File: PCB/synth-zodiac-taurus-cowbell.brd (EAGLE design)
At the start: 49 x 22 mm, 53 parts, among them Q1 NPN, Q2 NPN, SW1 Push Switch, SW2 Push Switch, U1 TL071, U2 ATTiny2313, X1 16MHz, X2 16MHz

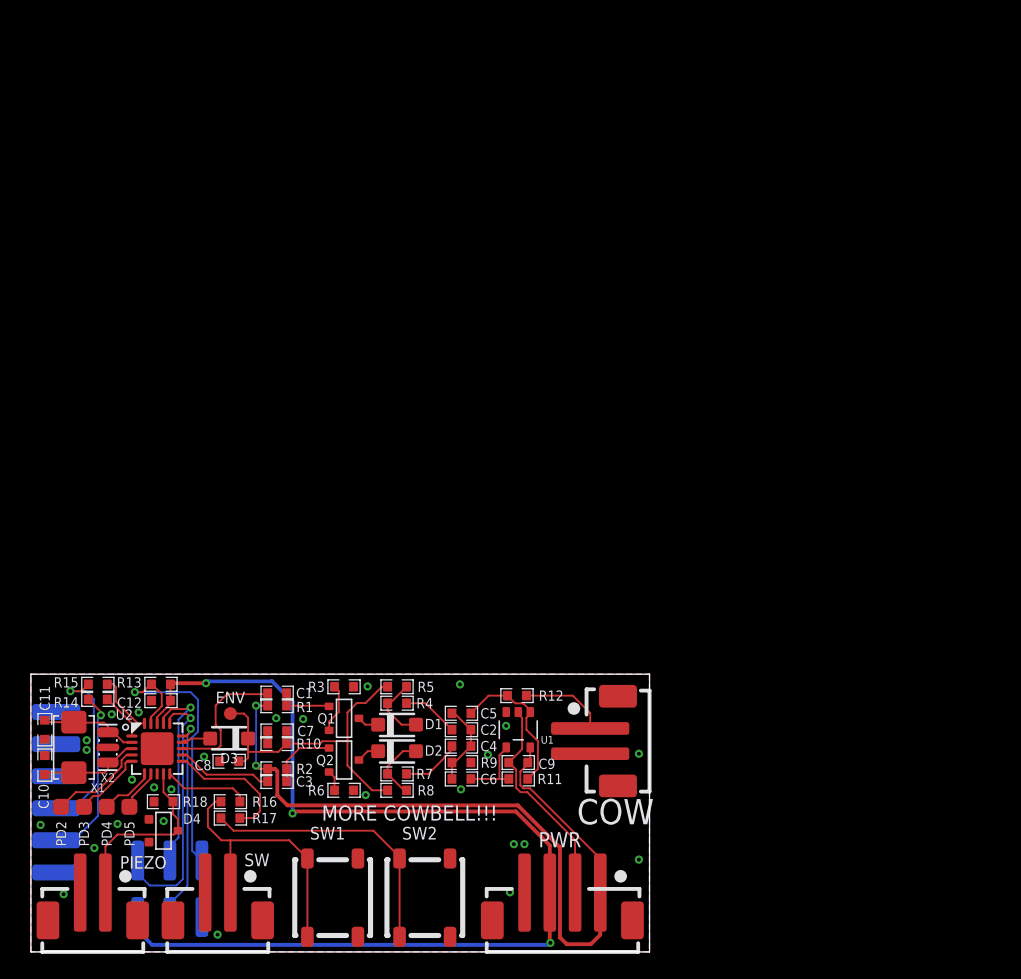
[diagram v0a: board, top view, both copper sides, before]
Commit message: Almost ready for FAB.
Sagittarius was mis-spelled, renamed it.  Taurus is still WIP.
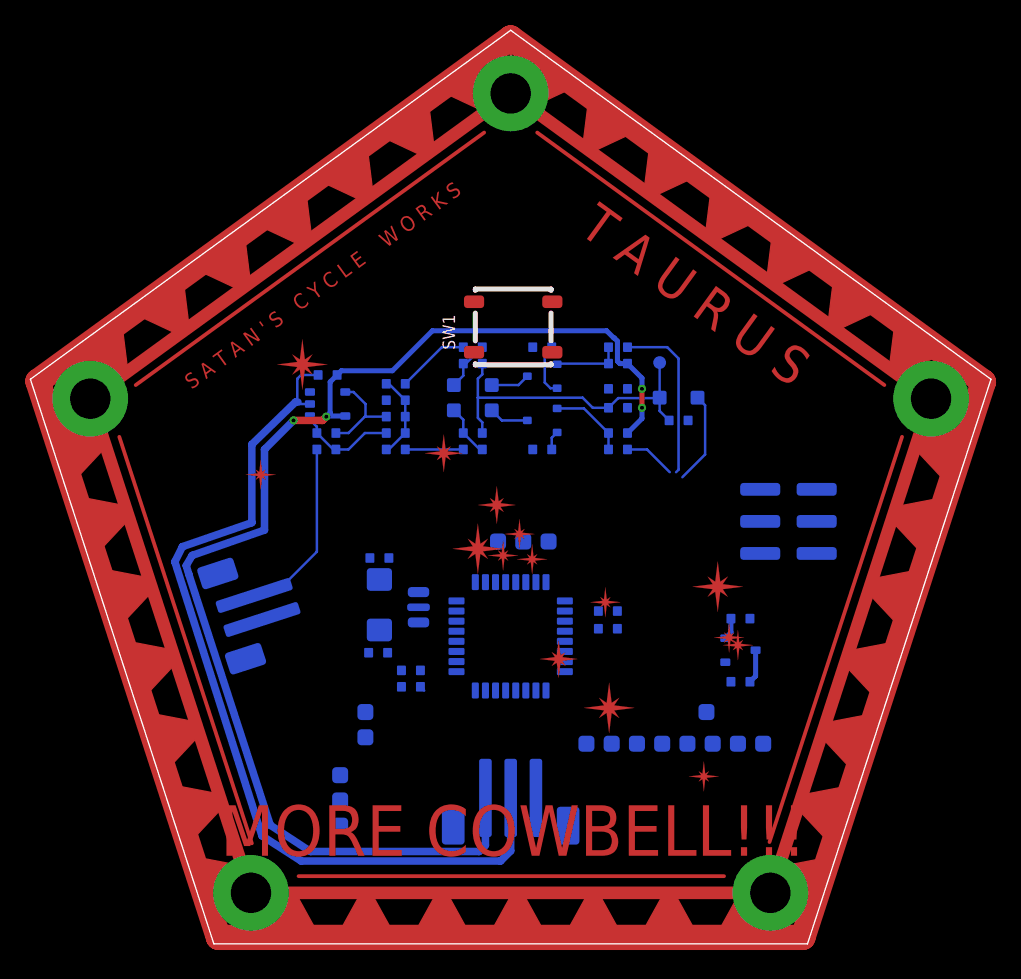
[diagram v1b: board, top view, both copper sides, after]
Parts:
- removed COW, PIEZO, SW: 2-pin, VT, SMT, con-jst:B2B-PH-SM4
- removed D4: Zener, xxxV, diodes:SOT-23
- removed FTDI: Header, 06P, con-headers:MA06X1-EDGE-2.54MM
- removed PD4, PD5: PADSMD-050X050, con-testpoints:SMD-050X050
- removed R14, R15, R17: 100, rlc:0603-RES
- removed R18: 1M, rlc:0603-RES
- removed SW2: Push Switch, switch-smd:B3SN
- removed U2: ATTiny2313, atmel-atmega:MLF20-JEDEC_MO-220
- added A0, A1, A2, A3, A4, A5, A6, A7, AREF, GND, PB0, PB1, PB2, RX, TX: PADSMD-050X050, con-testpoints:SMD-050X050
- added C13, C14: 1uF, rlc:0603-CAP
- added C15: 0.1uF, rlc:0603-CAP
- added CONST1: (no value), circuit-monkey-zodiac:TAURUS-CONST
- added COW2VCA: 2-pin, VT, SMT, con-jst:B2B-PH-SM4
- added PCB1: PCB FAB, circuit-monkey-zodiac:PENTAGON-40MM-RAD
- added U3: ATmega328P-AU, atmel-atmega:TQFP-32-08
- added VR: 5V, regulators:SOT-23
- PWR: value JST, 04P, VT, SMT -> JST, 3P, VT, SMT; device con-jst:B4B-PH-SM4 -> con-jst:B3B-PH-SM4
- moved ICSP 57.0 mm to (60.0, 34.1), turned to 90 degrees
- moved SW1 47.4 mm to (38.2, 49.5), turned to 0 degrees
- moved C8 44.7 mm to (51.3, 42.1), flipped to the bottom
- moved D3 44.7 mm to (51.3, 43.9), flipped to the bottom
- moved ENV 43.9 mm to (49.8, 46.7), flipped to the bottom
- moved C1 38.5 mm to (46.5, 47.9), flipped to the bottom
- moved C7 38.3 mm to (46.5, 44.6), flipped to the bottom
- moved R1 38.3 mm to (46.5, 46.6), flipped to the bottom
- moved R10 37.9 mm to (46.5, 43.1), flipped to the bottom
- moved R2 37.9 mm to (46.5, 41.1), flipped to the bottom
- moved C3 37.7 mm to (46.5, 39.8), flipped to the bottom
- moved C12 36.1 mm to (45.7, 27.0), flipped to the bottom
- moved R13 35.7 mm to (45.7, 25.6), flipped to the bottom
- moved C9 34.2 mm to (23.5, 45.7), flipped to the bottom, turned to 0 degrees
- moved R11 31.3 mm to (23.4, 41.1), flipped to the bottom
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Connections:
- removed net BTN_2: R17.1, U2.11
- removed net PIEZO: D4.3, PIEZO.1, R18.2, U2.9
- new net N$14: PD2.1, U3.32
- new net N$22: A3.1, U3.26
- new net N$23: A4.1, U3.27
- new net N$24: A5.1, U3.28
- new net N$25: A6.1, U3.19
- new net N$26: A7.1, U3.22
- new net N$27: AREF.1, U3.20
- net !RST: now also U3.29; no longer U2.19
- net +5V: now also C14.1, C15.1, U3.18, U3.4, U3.6, VR.2; no longer PWR.3, U2.18
- net +9V: now also C13.1, VR.3
- net BTN_1: now also U3.2; no longer U2.10
- net COW_OUT: now also COW2VCA.1; no longer COW.1
- net GND: now also C13.2, C14.2, C15.2, COW2VCA.2, GND.1, PCB1.MTG1, PCB1.MTG2, PCB1.MTG3, PCB1.MTG4, PCB1.MTG5, PWR.3, U3.21, U3.3, U3.5, VR.1; no longer COW.2, D4.1, FTDI.1, PIEZO.2, PWR.4, R18.1, SW.2, SW2.3, SW2.4, U2.8, U2.PAD
- net MISO: now also U3.16; no longer U2.16
- net MOSI: now also U3.15; no longer U2.15
- net N$11: no longer SW.1
- net N$12: now also PD3.1, U3.1; no longer R17.2, SW2.1, SW2.2
- net N$16: now also PB2.1, U3.14; no longer PD5.1, U2.7
- net N$17: now also PB1.1, U3.13; no longer PD4.1, U2.6
- net N$18: now also PB0.1, U3.12; no longer PD3.1, U2.5
- net N$19: now also A0.1, U3.23; no longer PD2.1, U2.4
- net N$20: now also A1.1, U3.24; no longer FTDI.5, R14.2
- net N$21: now also A2.1, U3.25; no longer FTDI.4, R15.2
- net PULSE_1MS: now also U3.11; no longer U2.14
- net RX: now also RX.1, U3.30; no longer R15.1, U2.20
- net SCK: now also U3.17; no longer U2.17
- net SQ_540: now also U3.9; no longer U2.12
- net SQ_800: now also U3.10; no longer U2.13
- net TX: now also TX.1, U3.31; no longer R14.1, U2.1
- net XTAL1: now also U3.7; no longer U2.3
- net XTAL2: now also U3.8; no longer U2.2
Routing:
- net +5V: track 86.4 -> 1.74 mm, vias 3 -> 0
- net -9V: track 17.4 -> 70.6 mm
- net +9V: track 62.5 -> 103.4 mm, vias 2 -> 4
- net !RST: track 23.9 -> 0.00 mm, vias 1 -> 0
- net N$11: track 21.9 -> 0.00 mm
- net N$12: track 21.8 -> 0.00 mm
- net MISO: track 20.6 -> 0.00 mm, vias 1 -> 0
- net MOSI: track 16.6 -> 0.00 mm, vias 1 -> 0
- net SCK: track 15.8 -> 0.00 mm, vias 1 -> 0
- net PIEZO: track 14.9 -> 0.00 mm
- net N$21: track 14.5 -> 0.00 mm, vias 1 -> 0
- net N$20: track 13.8 -> 0.00 mm, vias 1 -> 0
- net BTN_2: track 10.4 -> 0.00 mm
- net XTAL1: track 8.07 -> 0.00 mm
- net XTAL2: track 7.89 -> 0.00 mm
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- removed copper zone on layer 1, net GND
- removed copper zone on layer 16, net GND
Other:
- board size 49 x 22 mm -> 76.1 x 72.4 mm
- board text added: "Rev. B"
- board text added: "T A U R U S"
- board text removed: "Rev. A - 2022-06"
- board text removed: "Zodiac - Taurus - Cowbell Test Board"
- board text removed: "by Circuit Monkey"

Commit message: Work in progress for rev A,  VCO rev.B
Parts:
- removed R16: 100, rlc:0603-RES
- removed SW1: Push Switch, switch-smd:B3SN
- added C16, C17: 0.1uF, rlc:0603-CAP
- added COW: SPST, TACT, MOM, switch-smd:B3FS-BACKMOUNT
- added GLYPH1: (no value), circuit-monkey-zodiac:TAURUS-GLYPH
- added R14: 100, rlc:0603-RES
- added X3: 16MHz, xtal:32X25
- COW2VCA: value 2-pin, VT, SMT -> JST, SH, 2P; device con-jst:B2B-PH-SM4 -> con-jst:BM02B-SRSS-TB
- ICSP: value (none) -> Connector, 6P, SM, VT; device con-headers:MA03X2-VT-SMD -> con-jst:BM06B-SRSS-TB
- PWR: value JST, 3P, VT, SMT -> JST SM 3P; device con-jst:B3B-PH-SM4 -> con-jst:BM03B-SRSS-TB
- moved ICSP 31.3 mm to (37.8, 12.1), turned to 180 degrees
- moved PB2 25.1 mm to (16.1, 35.3), turned to 0 degrees
- moved PB1 23.0 mm to (16.1, 33.7), turned to 0 degrees
- moved A0 21.2 mm to (36.9, 18.6)
- moved PB0 20.9 mm to (16.1, 32.1), turned to 0 degrees
- moved A1 20.7 mm to (35.4, 18.6)
- moved A2 20.2 mm to (33.9, 18.6)
- moved A3 19.7 mm to (32.4, 18.6)
- moved A4 19.2 mm to (30.9, 18.6)
- moved A5 18.7 mm to (29.4, 18.6)
- moved AREF 18.6 mm to (35.7, 25.9)
- moved A6 18.2 mm to (27.9, 18.6)
- moved A7 17.7 mm to (26.4, 18.6)
- moved C7 17.0 mm to (61.0, 35.8), turned to 180 degrees
- moved Q2 16.8 mm to (55.8, 35.1)
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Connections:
- net !RST: now also C17.1
- net -9V: now also C16.2; no longer C9.2
- net BTN_1: now also R14.1; no longer R16.1
- net GND: now also C16.1, C17.2, C9.2, COW.3; no longer SW1.3, SW1.4
- net N$11: now also COW.1, R14.2; no longer R16.2, SW1.1, SW1.2
- net XTAL1: now also X3.1
- net XTAL2: now also X3.3
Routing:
- net SQ_540: track 4.09 -> 81.0 mm, vias 0 -> 2
- net PULSE_1MS: track 7.29 -> 76.7 mm, vias 0 -> 2
- net +5V: track 1.74 -> 63.0 mm
- net N$11: track 0.00 -> 56.7 mm
- net SQ_800: track 13.5 -> 63.7 mm, vias 0 -> 2
- net MISO: track 0.00 -> 22.2 mm, vias 0 -> 2
- net MOSI: track 0.00 -> 22.1 mm, vias 0 -> 2
- net +9V: track 103.4 -> 83.1 mm, vias 4 -> 0
- net !RST: track 0.00 -> 19.8 mm, vias 0 -> 2
- net SCK: track 0.00 -> 19.0 mm, vias 0 -> 2
- net N$16: track 0.00 -> 19.0 mm, vias 0 -> 2
- net N$17: track 0.00 -> 17.1 mm, vias 0 -> 2
- net N$25: track 0.00 -> 16.6 mm, vias 0 -> 2
- net N$18: track 0.00 -> 16.6 mm, vias 0 -> 2
- net COW_OUT: track 14.5 -> 30.5 mm
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- added copper zone on layer 1, net GND
- added copper zone on layer 16, net GND
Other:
- board text added: "Rev. A"
- board text removed: "Rev. B"
